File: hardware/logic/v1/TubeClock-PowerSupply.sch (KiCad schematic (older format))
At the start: 29 parts, among them J1 Jack-DC, Q1 IRF644PBF, U1 MAX1771, U2 LD1117S33TR

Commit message: Updated BoMs with more notes
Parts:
- F1: Part Number 2920L185DR -> 2920L050DR
- U2: Part Number LD1117ADT33TR -> LD1117S33TR
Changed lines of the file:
@@
 F 2 "Fuse:Fuse_2920_7451Metric" H 5650 900 50  0001 L CNN
 F 3 "http://m.littelfuse.com/~/media/electronics/datasheets/resettable_ptcs/littelfuse_ptc_2920l_datasheet.pdf.pdf" H 5600 1100 50  0001 C CNN
-F 4 "2920L185DR" V 5600 1100 60  0001 C CNN "Part Number"
+F 4 "2920L050DR" V 5600 1100 60  0001 C CNN "Part Number"
 	1    5600 1100
 	0    1    1    0
@@
 F 2 "Package_TO_SOT_SMD:TO-252-2" H 7600 3950 50  0001 C CNN
 F 3 "http://www.st.com/content/ccc/resource/technical/document/datasheet/a5/c3/3f/c9/2b/15/40/49/CD00002116.pdf/files/CD00002116.pdf/jcr:content/translations/en.CD00002116.pdf" H 7700 3500 50  0001 C CNN
-F 4 "LD1117ADT33TR" H 7600 3750 60  0001 C CNN "Part Number"
+F 4 "LD1117S33TR" H 7600 3750 60  0001 C CNN "Part Number"
 	1    7600 3750
 	1    0    0    -1

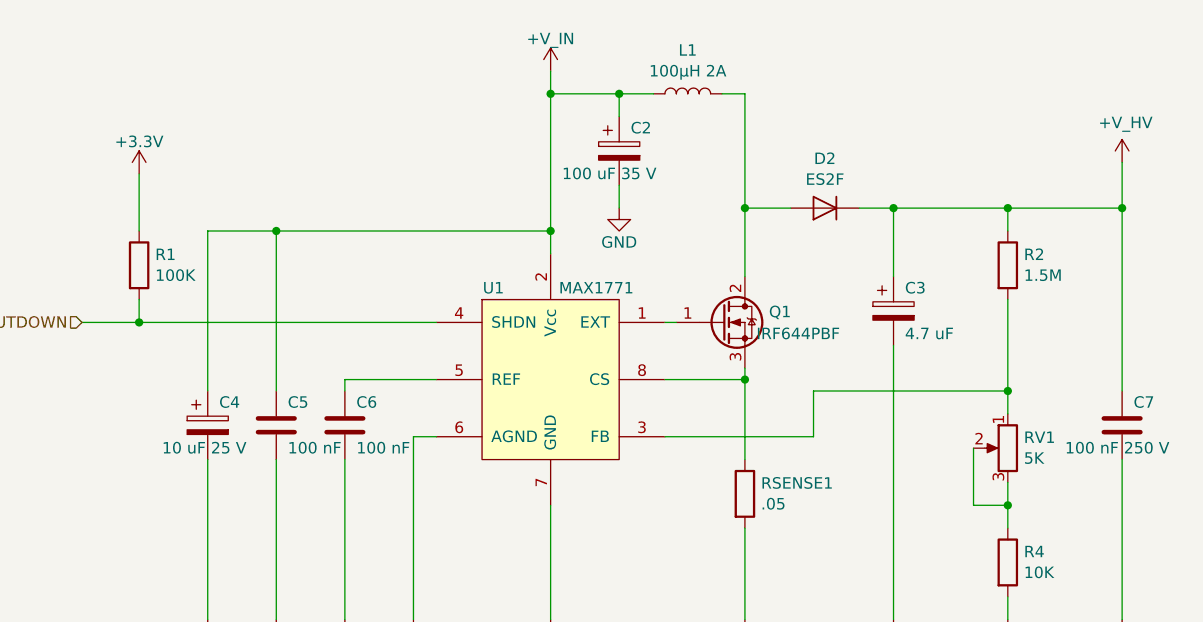
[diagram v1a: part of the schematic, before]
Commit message: Updated component specs
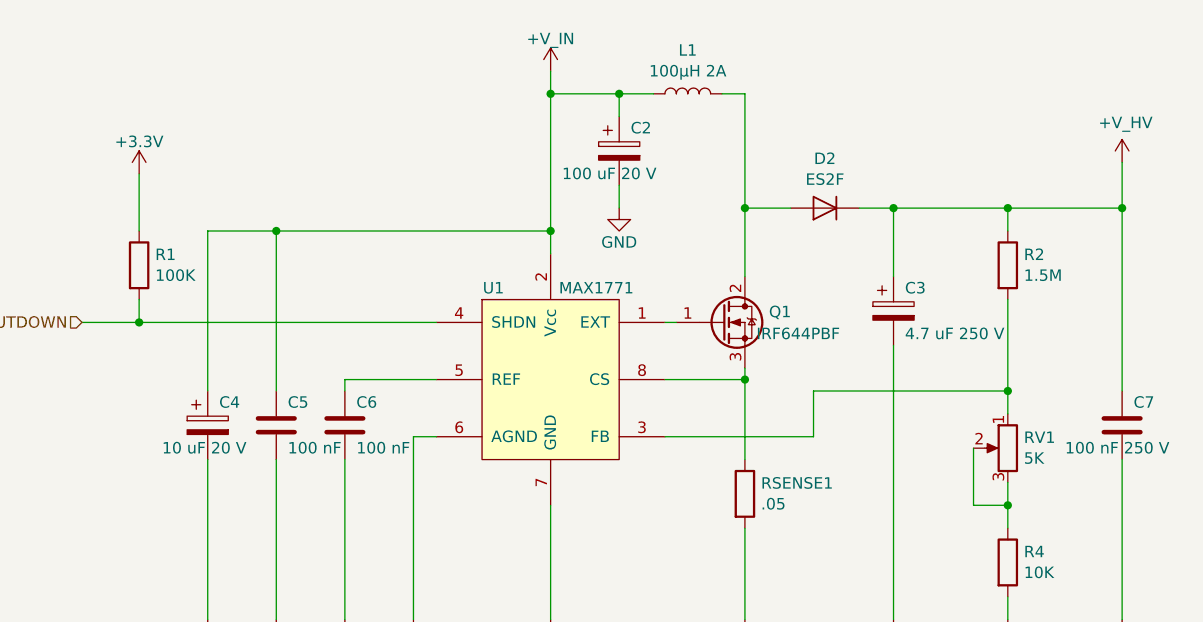
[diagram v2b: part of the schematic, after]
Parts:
- C2: value 100 uF 35 V -> 100 uF 20 V
- C3: value 4.7 uF -> 4.7 uF 250 V
- C4: value 10 uF 25 V -> 10 uF 20 V
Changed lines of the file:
@@
 P 3450 2650
 F 0 "C2" H 3500 2750 50  0000 L CNN
-F 1 "100 uF 35 V" H 3200 2550 50  0000 L CNN
+F 1 "100 uF 20 V" H 3200 2550 50  0000 L CNN
 F 2 "Capacitor_Tantalum_SMD:CP_EIA-7343-31_Kemet-D" H 3488 2500 50  0001 C CNN
 F 3 "~" H 3450 2650 50  0001 C CNN
@@
 P 1650 3850
 F 0 "C4" H 1700 3950 50  0000 L CNN
-F 1 "10 uF 25 V" H 1450 3750 50  0000 L CNN
+F 1 "10 uF 20 V" H 1450 3750 50  0000 L CNN
 F 2 "Capacitor_Tantalum_SMD:CP_EIA-7343-31_Kemet-D" H 1688 3700 50  0001 C CNN
 F 3 "~" H 1650 3850 50  0001 C CNN
@@
 P 4650 3350
 F 0 "C3" H 4700 3450 50  0000 L CNN
-F 1 "4.7 uF" H 4700 3250 50  0000 L CNN
+F 1 "4.7 uF 250 V" H 4700 3250 50  0000 L CNN
 F 2 "Capacitor_SMD:CP_Elec_10x10" H 4688 3200 50  0001 C CNN
 F 3 "~" H 4650 3350 50  0001 C CNN
